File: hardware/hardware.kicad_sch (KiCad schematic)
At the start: 0 parts

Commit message: mam dosc
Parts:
- added C1: 470 μ, bird-feeder:electrolytic_CAPPRD500W65D1000H2700, symbol bird-feeder:EEUFC0J222
- added C10, C4, C8: 10 μ, Capacitor_SMD:C_0603_1608Metric, symbol bird-feeder:C
- added C11, C12, C15: 1000 μ, bird-feeder:electrolytic_CAPPRD500W65D1000H2700, symbol bird-feeder:EEUFC0J222
- added C13, C3, C6, C7, C9: 1 μ, Capacitor_SMD:C_0603_1608Metric, symbol bird-feeder:C
- added C2: 1 n, bird-feeder:electrolytic_CAPPRD500W65D1000H2700, symbol bird-feeder:EEUFC0J222
- added C5: 100 μ, Capacitor_SMD:C_0603_1608Metric, symbol bird-feeder:C
- added D1, D2, D3: SS34, Diode_THT:D_DO-41_SOD81_P10.16mm_Horizontal, symbol bird-feeder:SB120
- added F1: Polyfuse, bird-feeder:polyfuse_FUSC7451X115N, symbol bird-feeder:Polyfuse
- added IC1: MC34063ABD-TR, bird-feeder:MC34063A_SOIC127P600X175-8N, symbol bird-feeder:MC34063ABD-TR
- added IC2: TLV1117LV33DCYR, bird-feeder:SOT230P700X180-4N, symbol bird-feeder:TLV1117LV33DCYR
- added IC3: TPS61085TDGKR, bird-feeder:SOP65P490X110-8N, symbol bird-feeder:TPS61085TDGKR
- added J1: Li-Po battery, bird-feeder:ARK raster 2,54 mm, symbol bird-feeder:Screw_Terminal_01x02
- added J10: pin_2, bird-feeder:pin_2_RHDR4W60P0X254_1X4_1016X250X840P_1, symbol bird-feeder:pin_2
- added J2: left side, bird-feeder:pin_8_RHDR4W60P0X254_1X4_1016X250X840P_1, symbol bird-feeder:pin_8
- added J3: right side, bird-feeder:pin_8_RHDR4W60P0X254_1X4_1016X250X840P_1, symbol bird-feeder:pin_8
- added J4, J7: Solar panel, bird-feeder:ARK raster 2,54 mm, symbol bird-feeder:Screw_Terminal_01x02
- added J5: servo, bird-feeder:pin_4_RHDR4W60P0X254_1X4_1016X250X840P, symbol bird-feeder:pin_4
- added J6: 5V_DC/DC, bird-feeder:pin_2_RHDR4W60P0X254_1X4_1016X250X840P_1, symbol bird-feeder:pin_2
- added J8: ultrasonic, bird-feeder:pin_4_RHDR4W60P0X254_1X4_1016X250X840P, symbol bird-feeder:pin_4
- added J9: UART, bird-feeder:pin_4_RHDR4W60P0X254_1X4_1016X250X840P, symbol bird-feeder:pin_4
- added L1: 100 μ, symbol Device:L_Iron
- added LED1: 3.3 V, bird-feeder:LEDC2012X40N, symbol bird-feeder:LS_R976
- added LED2: 5 V, bird-feeder:LEDC2012X40N, symbol bird-feeder:LS_R976
- added Q1, Q2: IRLML2502TRPBF, bird-feeder:IRL_SOT95P237X112-3N, symbol bird-feeder:IRLML2502TRPBF
- added R1: 180, Resistor_SMD:R_0603_1608Metric, symbol bird-feeder:R
- added R10, R7: 100 k, Resistor_SMD:R_0603_1608Metric, symbol bird-feeder:R
- added R11: 10 k, Resistor_SMD:R_0603_1608Metric, symbol bird-feeder:R
- added R12: 20 k, Resistor_SMD:R_0603_1608Metric, symbol bird-feeder:R
- added R2: 0.22, Resistor_SMD:R_0603_1608Metric, symbol bird-feeder:R
- added R3: 3 k, Resistor_SMD:R_0603_1608Metric, symbol bird-feeder:R
- added R4: 1 k, Resistor_SMD:R_0603_1608Metric, symbol bird-feeder:R
- added R5, R6: 470, Resistor_SMD:R_0603_1608Metric, symbol bird-feeder:R
- added R8, R9: 100, Resistor_SMD:R_0603_1608Metric, symbol bird-feeder:R
- added U1: TP4056, bird-feeder:TP4056, symbol bird-feeder:TP4056
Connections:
- new net: LED2.2 (A), R6.2
- new net: J2.3, R7.2, R8.1
- new net: J2.4, R10.2, R9.1
- new net: J2.6, R11.2, R12.1
- new net: Q2.1 (G), R9.2
- new net: C2.1 (+), IC1.3 (TC)
- new net: J1.1 (Pin_1), U1.4 (B_+)
- new net: D1.1 (K), D3.1 (K), F1.2
- new net: D1.2 (A), J4.1 (Pin_1)
- new net: Q1.1 (G), R8.2
- new net: D2.2 (A), IC1.1 (SWC), L1.2
- new net: IC1.7 (IPK), L1.1, R1.1, R2.2
- new net: IC1.5 (CII), R3.1, R4.1
- new net: IC1.8 (DRC), R1.2
- new net: LED1.2 (A), R5.2
- new net: D3.2 (A), J7.1 (Pin_1)
- new net: J3.3, J3.4
- new net +3.3V: IC2.2 (OUT_1), IC2.4 (OUT_2), R5.1
- new net +5V: C11.1 (+), C12.1 (+), C13.1, C15.1 (+), C3.1, C4.1, C5.1, C6.1, C8.1, D2.1 (K), IC2.3 (INPUT), J10.1, J2.1, J5.2, J6.1, J6.2, J8.1, J9.2, R3.2, R6.1
- new net GND: C1.2 (-), C10.2, C11.2 (-), C12.2 (-), C13.2, C15.2 (-), C2.2 (-), C3.2, C4.2, C5.2, C6.2, C7.2, C8.2, C9.2, IC1.2 (SWE), IC1.4 (GND), IC2.1 (GND), J1.2 (Pin_2), J2.2, J3.8, J4.2 (Pin_2), J7.2 (Pin_2), J8.4, J9.1, LED1.1 (K), LED2.1 (K), Q1.2 (S), Q2.2 (S), R10.1, R12.2, R4.2, R7.1, U1.2 (-), U1.5 (B_-), U1.6 (OUT_-)
- new net LED: J2.8
- new net MOSFET_LED: J10.2, Q1.3 (D)
- new net MOSFET_servo: J5.3, Q2.3 (D)
- new net TP_in: C9.1, F1.1, U1.1 (+)
- new net UOR: J3.6, J9.3
- new net UOT: J3.7, J9.4
- new net char_out+: C1.1 (+), C10.1, C7.1, IC1.6 (VCC), R2.1, U1.3 (OUT_+)
- new net echo: J8.2, R11.1
- new net servo_PWM: J2.7, J5.1
- new net trig: J2.5, J8.3
- no-connect marks 0 -> 4
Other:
- note added: "3.3 V STABILIZATION"
- note added: "BACK-BOOST 5 V"
- note added: "BATTERY CHARGER VIA SOLAR"
- note added: "DECOUPLING CAPS"
- note added: "ESP"
- note added: "ESP32-CAM CONNECTION"
- note added: "HC-SR04"
- note added: "LED"
- note added: "PERIPHERY"
- note added: "dodac te wyprowadzneia 2 do bom"
- note added: "servo"
- note added: "znalezc cewke i jej footprint"

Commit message: aleluja i do poniedzialku
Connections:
- net MOSFET_LED is gone; now on net +5V: J10.2, Q1.3 (D)
- net MOSFET_servo is gone; now on net +5V: J5.3, Q2.3 (D)
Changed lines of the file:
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@@
 	)
 	(junction
+		(at 170.18 21.59)
+		(diameter 0)
+		(color 0 0 0 0)
+	)
+	(junction
 		(at 217.17 30.48)
 		(diameter 0)
@@
 	)
 	(junction
+		(at 144.78 41.91)
+		(diameter 0)
+		(color 0 0 0 0)
+	)
+	(junction
 		(at 29.21 109.22)
 		(diameter 0)
@@
 	(wire
 		(pts
+			(xy 144.78 38.1) (xy 144.78 41.91)
+		)
+		(stroke
+			(width 0)
+			(type default)
+		)
+	)
+	(wire
+		(pts
 			(xy 241.3 64.77) (xy 242.57 64.77)
 		)
@@
 	(wire
 		(pts
+			(xy 170.18 19.05) (xy 170.18 21.59)
+		)
+		(stroke
+			(width 0)
+			(type default)
+		)
+	)
+	(wire
+		(pts
 			(xy 250.19 137.16) (xy 250.19 139.7)
 		)
@@
 	)
 	(symbol
+		(lib_id "power:+5V")
+		(at 144.78 38.1 0)
+		(unit 1)
+		(exclude_from_sim no)
+		(in_bom yes)
+		(on_board yes)
+		(dnp no)
+		(property "Reference" "#PWR014"
+			(at 144.78 41.91 0)
+			(effects
+				(font
+					(size 1.27 1.27)
+				)
+				(hide yes)
+			)
+		)
+		(property "Value" "+5V"
+			(at 141.986 34.798 0)
+			(effects
+				(font
+					(size 1.27 1.27)
+				)
+			)
+		)
+		(property "Footprint" ""
+			(at 144.78 38.1 0)
+			(effects
+				(font
+					(size 1.27 1.27)
+				)
+				(hide yes)
+			)
+		)
+		(property "Datasheet" ""
+			(at 144.78 38.1 0)
+			(effects
+				(font
+					(size 1.27 1.27)
+				)
+				(hide yes)
+			)
+		)
+		(property "Description" "Power symbol creates a global label with name \"+5V\""
+			(at 144.78 38.1 0)
+			(effects
+				(font
+					(size 1.27 1.27)
+				)
+				(hide yes)
+			)
+		)
+		(pin "1"
+		)
+		(instances
+			(project "hardware"
+				(path "/ddfcea42-4758-4332-a0ef-c23f819ebcba"
+					(reference "#PWR014")
+					(unit 1)
+				)
+			)
+		)
+	)
+	(symbol
 		(lib_id "power:GND")
 		(at 144.78 64.77 0)
@@
 					(unit 1)
 				)
+			)
+		)
+	)
+	(symbol
+		(lib_id "power:+5V")
+		(at 170.18 19.05 0)
+		(unit 1)
+		(exclude_from_sim no)
+		(in_bom yes)
+		(on_board yes)
+		(dnp no)
+		(property "Reference" "#PWR025"
+			(at 170.18 22.86 0)
+			(effects
+				(font
+					(size 1.27 1.27)
+				)
+				(hide yes)
+			)
+		)
+		(property "Value" "+5V"
+			(at 166.878 16.764 0)
+			(effects
+				(font
+					(size 1.27 1.27)
+				)
+			)
+		)
+		(property "Footprint" ""
+			(at 170.18 19.05 0)
+			(effects
+				(font
+					(size 1.27 1.27)
+				)
+				(hide yes)
+			)
+		)
+		(property "Datasheet" ""
+			(at 170.18 19.05 0)
+			(effects
+				(font
+					(size 1.27 1.27)
+				)
+				(hide yes)
+			)
+		)
+		(property "Description" "Power symbol creates a global label with name \"+5V\""
+			(at 170.18 19.05 0)
+			(effects
+				(font
+					(size 1.27 1.27)
+				)
+				(hide yes)
+			)
+		)
+		(pin "1"
+		)
+		(instances
+			(project "hardware"
+				(path "/ddfcea42-4758-4332-a0ef-c23f819ebcba"
+					(reference "#PWR025")
+					(unit 1)
+				)

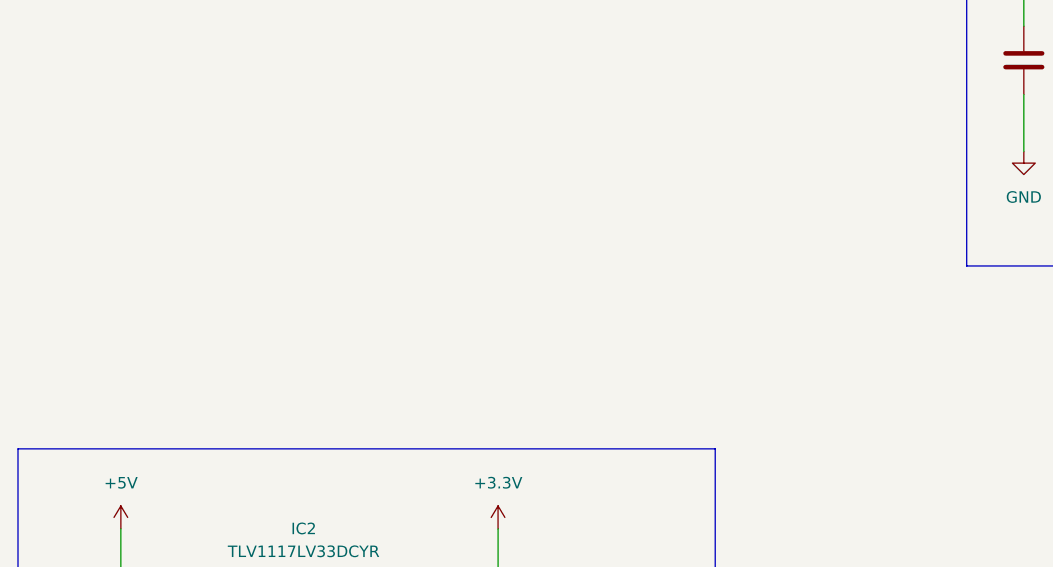
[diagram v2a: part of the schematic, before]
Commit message: jazda z dc/dc
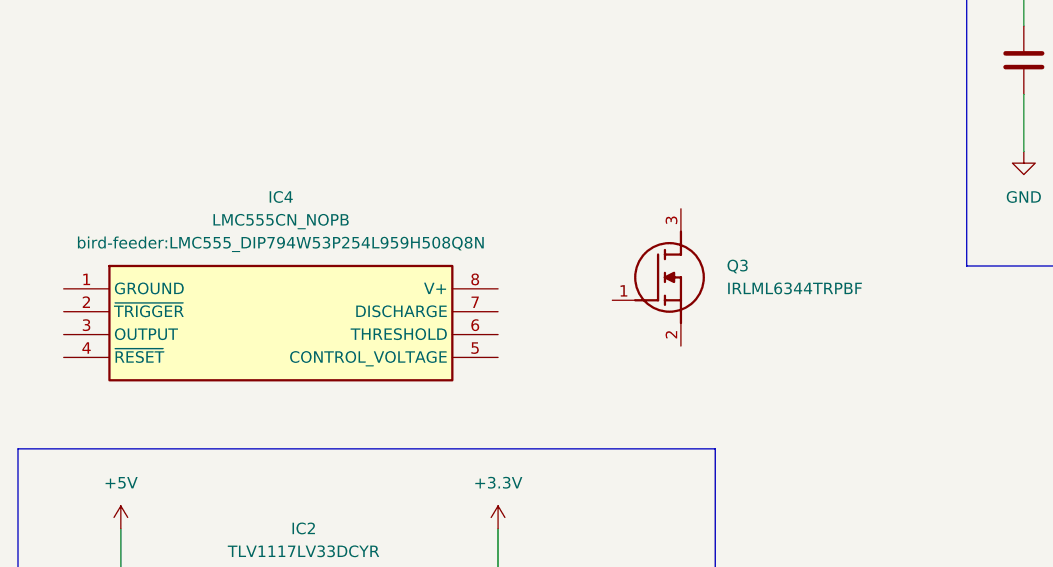
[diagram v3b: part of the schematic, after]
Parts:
- added IC4: LMC555CN_NOPB, bird-feeder:LMC555_DIP794W53P254L959H508Q8N, symbol bird-feeder:LMC555CN_NOPB
- added Q3: IRLML6344TRPBF, bird-feeder:I_SOT95P237X112-3N, symbol bird-feeder:IRLML6344TRPBF

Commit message: dobranoc
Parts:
- removed C1: 470 μ, bird-feeder:electrolytic_CAPPRD500W65D1000H2700, symbol bird-feeder:EEUFC0J222
- removed C2: 1 n, bird-feeder:electrolytic_CAPPRD500W65D1000H2700, symbol bird-feeder:EEUFC0J222
- removed C7: 1 μ, Capacitor_SMD:C_0603_1608Metric, symbol bird-feeder:C
- removed C8: 10 μ, Capacitor_SMD:C_0603_1608Metric, symbol bird-feeder:C
- removed IC1: MC34063ABD-TR, bird-feeder:MC34063A_SOIC127P600X175-8N, symbol bird-feeder:MC34063ABD-TR
- removed IC3: TPS61085TDGKR, bird-feeder:SOP65P490X110-8N, symbol bird-feeder:TPS61085TDGKR
- removed R3: 3 k, Resistor_SMD:R_0603_1608Metric, symbol bird-feeder:R
- removed R4: 1 k, Resistor_SMD:R_0603_1608Metric, symbol bird-feeder:R
- added C1, C2: 1 n, Capacitor_SMD:C_0603_1608Metric, symbol bird-feeder:C
- added D4: 1N4148, Diode_THT:D_DO-35_SOD27_P7.62mm_Horizontal, symbol Diode:1N4148
- added Z1: 1SMB5918BT3G, bird-feeder:zenner_DIOM5436X247N, symbol bird-feeder:1SMB5918BT3G
- Q3: value IRLML6344TRPBF -> IRLML2502; footprint bird-feeder:I_SOT95P237X112-3N -> bird-feeder:IRLML2502_SOT95P237X112-3N
- R1: value 180 -> 2.2 k
- R2: value 0.22 -> 12 k
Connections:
- net +3.3V: now also IC4.8 (V+), R1.2
- net +5V: now also LED2.2 (A), Z1.2 (A); no longer C6.1, IC2.3 (INPUT), R6.1
- net GND: now also IC4.1 (GND), Q3.2 (S), R6.2, C1.2, C2.2, Z1.1 (K); no longer LED2.1 (K)
- net char_out+: now also C6.1, IC2.3 (INPUT), L1.2; no longer R2.1
- net PWM: now reaches Q3.1 (G)
- net PWM: now also IC4.3 (OUT)
- net at Q3.3 (D): now also D2.2 (A), L1.1
- net at IC4.2 (~{TRIG}): now also IC4.5 (CV), IC4.6 (THRS), R2.1, C1.1, C2.1, D4.1 (K)
- net at IC4.7 (DIS): now also R1.1, R2.2, D4.2 (A)
- new net: LED2.1 (K), R6.1
- no-connect marks 4 -> 5
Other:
- note added: "BOOST 5 V"
- note added: "PWM GENERATION"
- note removed: "BACK-BOOST 5 V"
- moved on the sheet: C11, C6, D2, IC2, IC4, L1, LED1, LED2, Q3, R5, R6

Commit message: :c
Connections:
- net +5V: no longer J10.2, J5.3, Q1.3 (D), Q2.3 (D)
- new net LED_GND: J10.2, Q1.3 (D)
- new net servo_GND: J5.3, Q2.3 (D)
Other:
- note added: "PWM GENERATION FOR BOOST"
- note removed: "PWM GENERATION"
- moved on the sheet: C1, C11, C2, C6, D2, D4, IC2, IC4, J6, L1, LED1, LED2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

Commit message: open lab
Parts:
- removed C6, C9: 1 μ, Capacitor_SMD:C_0603_1608Metric, symbol bird-feeder:C
- removed D4: 1N4148, Diode_THT:D_DO-35_SOD27_P7.62mm_Horizontal, symbol Diode:1N4148
- removed IC2: TLV1117LV33DCYR, bird-feeder:SOT230P700X180-4N, symbol bird-feeder:TLV1117LV33DCYR
- removed L1: 100 μ, symbol Device:L_Iron
- removed LED1: 3.3 V, bird-feeder:LEDC2012X40N, symbol bird-feeder:LS_R976
- removed Q3: IRLML2502, bird-feeder:IRLML2502_SOT95P237X112-3N, symbol bird-feeder:IRLML6344TRPBF
- removed R5: 470, Resistor_SMD:R_0603_1608Metric, symbol bird-feeder:R
- removed Z1: 1SMB5918BT3G, bird-feeder:zenner_DIOM5436X247N, symbol bird-feeder:1SMB5918BT3G
- added R3: 470, Resistor_SMD:R_0603_1608Metric, symbol bird-feeder:R
- added Z2: 1SMB5918BT3G, bird-feeder:zenner_DIOM5436X247N, symbol bird-feeder:1SMB5918BT3G
- C11: value 1000 μ -> 4700 μ
- D2: value SS34 -> 1N5818
- IC4: value LMC555CN_NOPB -> NE555; footprint bird-feeder:LMC555_DIP794W53P254L959H508Q8N -> bird-feeder:NE555_SOIC127P600X175-8N
- R1: value 2.2 k -> 1 k
- R2: value 12 k -> 15 k
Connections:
- net +3.3V is gone; now on net BAT: IC4.8 (V+), R1.2
- net char_out+ is gone; now on net BAT: C10.1, U1.3 (OUT_+)
- net +5V: now also Z2.1 (K)
- net GND: now also R3.2; no longer J1.2 (Pin_2), J4.2 (Pin_2), J7.2 (Pin_2), U1.2 (-), U1.5 (B_-)
- net at C1.1, IC4.2 (~{TRIG}), IC4.6 (THRS)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: no longer C2.1, IC4.5 (CV)
- net BAT: now reaches IC4.4 (~{RST})
- net LED: no longer names the net of J2.8
- net TP_in: no longer names the net of F1.1, U1.1 (+)
- new net: R3.1, Z2.2 (A)
- new net: J1.2 (Pin_2), U1.5 (B_-)
- new net: C2.1, IC4.5 (CV)
- new net: J4.2 (Pin_2), J7.2 (Pin_2), U1.2 (-)
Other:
- note added: "PWM GENERATION"
- note added: "dodac te wyprowadzneia 2 do bom i model 3D do footprintu"
- note added: "znalezc cewke i jej footprint a potem MOSFET"
- note removed: "3.3 V STABILIZATION"
- note removed: "PWM GENERATION FOR BOOST"
- note removed: "dodac te wyprowadzneia 2 do bom"
- note removed: "znalezc cewke i jej footprint"
- moved on the sheet: C10, C11, C12, C13, C15, C2, C3, C4, C5, D2, IC4, LED2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

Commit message: lecisz z tym Janek
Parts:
- added R4: 100, Resistor_SMD:R_0603_1608Metric, symbol bird-feeder:R
- added R5: 10 k, Resistor_SMD:R_0603_1608Metric, symbol bird-feeder:R
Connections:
- net GND: now also R5.2
- net PWM: now also R4.1
- new net: R4.2, R5.1

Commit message: za Janka
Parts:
- removed C12, C15: 1000 μ, bird-feeder:electrolytic_CAPPRD500W65D1000H2700, symbol bird-feeder:EEUFC0J222
- removed C13: 1 μ, Capacitor_SMD:C_0603_1608Metric, symbol bird-feeder:C
- removed C4: 10 μ, Capacitor_SMD:C_0603_1608Metric, symbol bird-feeder:C
- removed C5: 100 μ, Capacitor_SMD:C_0603_1608Metric, symbol bird-feeder:C
- removed F1: Polyfuse, bird-feeder:polyfuse_FUSC7451X115N, symbol bird-feeder:Polyfuse
- removed J10: pin_2, bird-feeder:pin_2_RHDR4W60P0X254_1X4_1016X250X840P_1, symbol bird-feeder:pin_2
- removed J2: left side, bird-feeder:pin_8_RHDR4W60P0X254_1X4_1016X250X840P_1, symbol bird-feeder:pin_8
- removed J3: right side, bird-feeder:pin_8_RHDR4W60P0X254_1X4_1016X250X840P_1, symbol bird-feeder:pin_8
- removed J5: servo, bird-feeder:pin_4_RHDR4W60P0X254_1X4_1016X250X840P, symbol bird-feeder:pin_4
- removed J6: 5V_DC/DC, bird-feeder:pin_2_RHDR4W60P0X254_1X4_1016X250X840P_1, symbol bird-feeder:pin_2
- removed J8: ultrasonic, bird-feeder:pin_4_RHDR4W60P0X254_1X4_1016X250X840P, symbol bird-feeder:pin_4
- removed J9: UART, bird-feeder:pin_4_RHDR4W60P0X254_1X4_1016X250X840P, symbol bird-feeder:pin_4
- removed Q2: IRLML2502TRPBF, bird-feeder:IRL_SOT95P237X112-3N, symbol bird-feeder:IRLML2502TRPBF
- removed R4, R8, R9: 100, Resistor_SMD:R_0603_1608Metric, symbol bird-feeder:R
- removed R5: 10 k, Resistor_SMD:R_0603_1608Metric, symbol bird-feeder:R
- removed R7: 100 k, Resistor_SMD:R_0603_1608Metric, symbol bird-feeder:R
- added C6: 100 μ, Capacitor_SMD:C_0603_1608Metric, symbol bird-feeder:C
- added C7: 1 μ, Capacitor_SMD:C_0603_1608Metric, symbol bird-feeder:C
- added D7: 1N4148, Diode_THT:D_DO-35_SOD27_P7.62mm_Horizontal, symbol Diode:1N4148
- added D9: D_Zener, symbol Device:D_Zener
- added J11: pin_2, bird-feeder:pin_2_RHDR4W60P0X254_1X4_1016X250X840P_1, symbol bird-feeder:pin_2
- added J12: servo, bird-feeder:pin_4_RHDR4W60P0X254_1X4_1016X250X840P, symbol bird-feeder:pin_4
- added J13: UART, bird-feeder:pin_4_RHDR4W60P0X254_1X4_1016X250X840P, symbol bird-feeder:pin_4
- added J14: ultrasonic, bird-feeder:pin_4_RHDR4W60P0X254_1X4_1016X250X840P, symbol bird-feeder:pin_4
- added J19: ESP, bird-feeder:ARK raster 2,54 mm, symbol bird-feeder:Screw_Terminal_01x02
- added J2: Screw_Terminal_01x02, bird-feeder:ARK raster 2,54 mm, symbol bird-feeder:Screw_Terminal_01x02
- added J3: 5V_DC/DC, bird-feeder:pin_2_RHDR4W60P0X254_1X4_1016X250X840P_1, symbol bird-feeder:pin_2
- added L1: ETQP4M150KFN, bird-feeder:DE1207, symbol ETQP4M150KFN:ETQP4M150KFN
- added Q3: IRF740, Library:IRF740, symbol IRF740:IRF740
- added Q5: BD911, Package_TO_SOT_THT:TO-220-3_Vertical, symbol Transistor_BJT:BD911
- added R13, R20: 10k, Resistor_THT:R_Axial_DIN0204_L3.6mm_D1.6mm_P5.08mm_Horizontal, symbol bird-feeder:R
- added R14: 20k, Resistor_THT:R_Axial_DIN0204_L3.6mm_D1.6mm_P5.08mm_Horizontal, symbol bird-feeder:R
- added R19: 100, Resistor_SMD:R_0603_1608Metric, symbol bird-feeder:R
- added R21: R, Resistor_SMD:R_0603_1608Metric, symbol bird-feeder:R
- added U3: ESP32-CAM, Library:ESP32-CAM, symbol ESP32-CAM:ESP32-CAM
- C10: footprint Capacitor_SMD:C_0603_1608Metric -> Capacitor_THT:CP_Axial_L10.0mm_D4.5mm_P15.00mm_Horizontal
- C11: value 4700 μ -> 1000u
- C3: value 1 μ -> 10 μ
- IC4: footprint bird-feeder:NE555_SOIC127P600X175-8N -> bird-feeder:LMC555_DIP794W53P254L959H508Q8N
- R1: value 1 k -> 10k
- R10: value 100 k -> 100k; footprint Resistor_SMD:R_0603_1608Metric -> Resistor_THT:R_Axial_DIN0204_L3.6mm_D1.6mm_P5.08mm_Horizontal
- R11: value 10 k -> 100k; footprint Resistor_SMD:R_0603_1608Metric -> Resistor_THT:R_Axial_DIN0204_L3.6mm_D1.6mm_P5.08mm_Horizontal
- R12: value 20 k -> 100
- R2: value 15 k -> 22 k
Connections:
- net LED_GND is gone; now on net servo_GND: Q1.3 (D)
- net +5V: now also C6.1, C7.1, J12.2, J13.2, J14.1, J19.1 (Pin_1), J2.1 (Pin_1), J3.1, J3.2, U3.P$1 (5V)
- net BAT: now also L1.2
- net GND: now also R10.2, C6.2, C7.2, J11.2, J13.1, J14.4, J19.2 (Pin_2), J2.2 (Pin_2), Q3.S, Q5.3 (E), R14.2, R20.2, R21.2, U3.P$2 (GND), U3.P$9 (.GND); no longer R10.1, R12.2
- net PWM: now also R19.1
- net UOR: now also J13.3, U3.P$11 (IO3/U0R)
- net UOT: now also J13.4, U3.P$10 (IO1/U0T)
- net echo: now also J14.2, R13.1; no longer R11.1
- net servo_GND: now also J12.3
- net servo_PWM: now also J12.1, U3.P$7 (IO2)
- net trig: now also J14.3, U3.P$5 (IO15)
- net at C1.1, IC4.2 (~{TRIGGER}), IC4.6 (THRESHOLD)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: now also D7.1 (K)
- net at R11.2: now also Q1.1 (G), R10.1; no longer R12.1
- net at D1.1 (K), D3.1 (K): now also U1.1 (+)
- net at IC4.7 (DISCHARGE), R1.1, R2.2: now also D7.2 (A)
- net at D2.2 (A): now also L1.1, Q3.D
- new net: R11.1, U3.P$4 (IO13)
- new net: Q3.G, R19.2, R20.1
- new net: R13.2, R14.1, U3.P$6 (IO14)
- new net: D9.2 (A), Q5.1 (B)
- new net: D9.1 (K), R21.1
- new net: U3.P$13 (GND.), U3.P$14 (IO0)
- new net: R12.1, U3.P$3 (IO12)
- new net CONTROL_VOLTAGE: Q5.2 (C)
- new net LED_Vcc: J11.1, R12.2
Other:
- added sheet esp+peryferia (esp+peryferia.kicad_sch)
- added sheet zasilanie (zasilanie.kicad_sch)
- note added: "NEGATIVE FEEDBACK LOOP"
- note removed: "LED"
- moved on the sheet: IC4, R1
